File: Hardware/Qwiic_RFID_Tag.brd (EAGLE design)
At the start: 30.5 x 44.5 mm, 50 parts, among them J1 Qwiic, J2 Qwiic, U1 ST25DV64KC

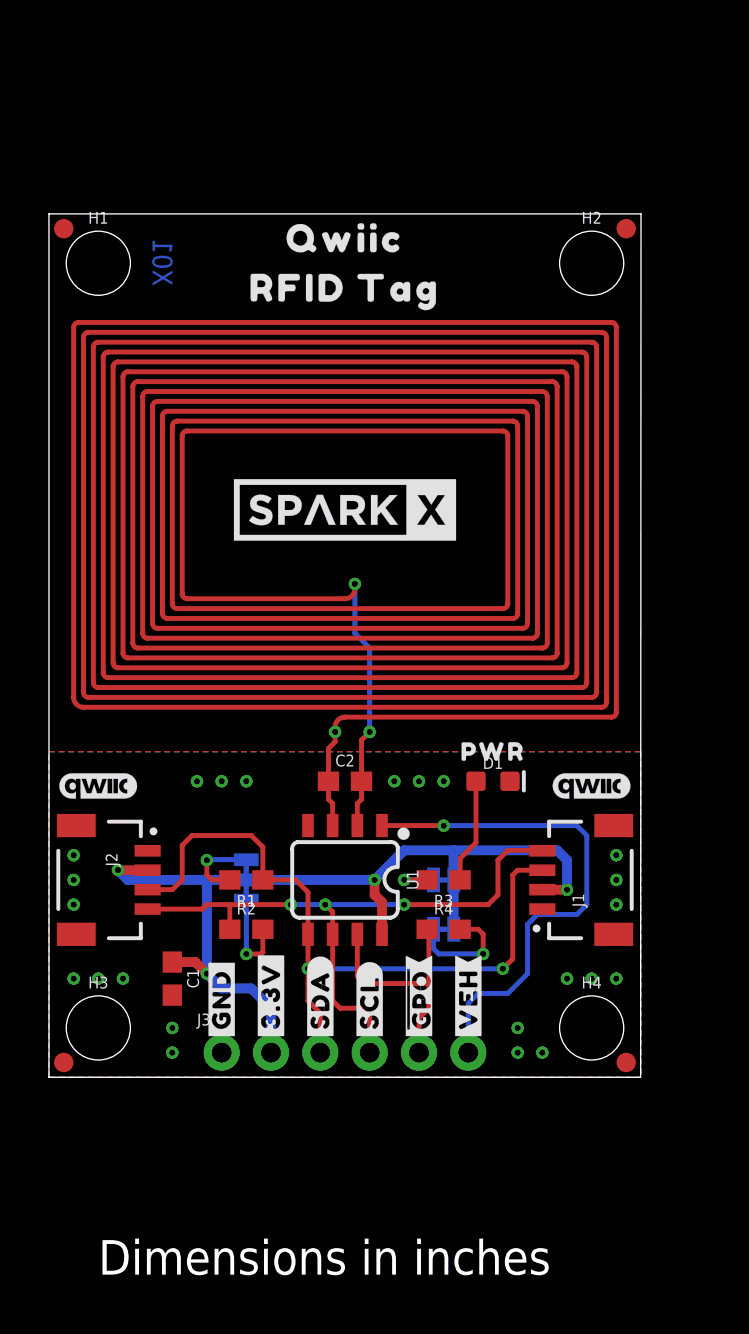
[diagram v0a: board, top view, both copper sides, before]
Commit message: Fixed fiducial placement, board version size and polygon isolation.
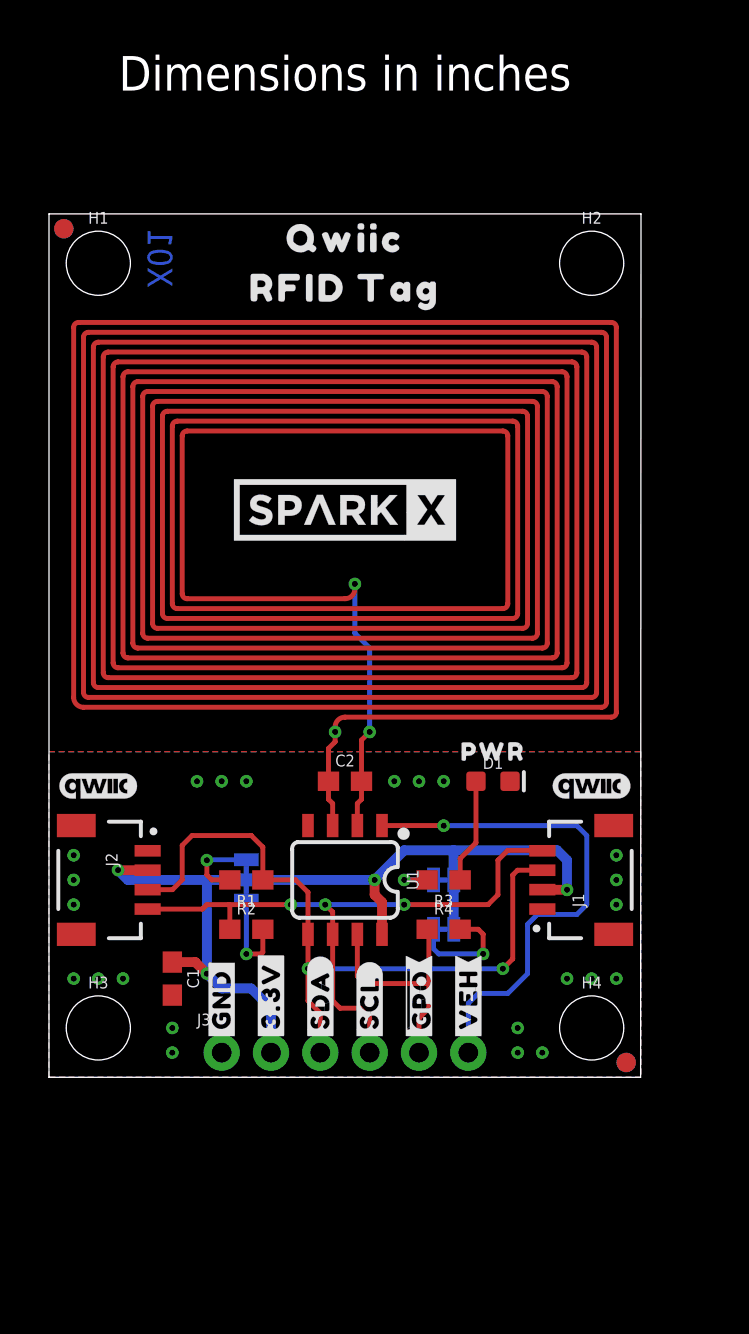
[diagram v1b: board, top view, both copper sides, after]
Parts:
- moved FD1 29.0 mm to (0.76, 43.7), flipped to the bottom
- moved FD3 29.0 mm to (29.7, 0.76), flipped to the bottom
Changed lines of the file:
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@@
 <drawing>
 <settings>
-<setting alwaysvectorfont="no"/>
+<setting alwaysvectorfont="yes"/>
 <setting verticaltext="up"/>
 </settings>
-<grid distance="0.05" unitdist="inch" unit="inch" style="lines" multiple="1" display="yes" altdistance="0.005" altunitdist="inch" altunit="inch"/>
+<grid distance="0.1" unitdist="inch" unit="inch" style="lines" multiple="1" display="yes" altdistance="0.005" altunitdist="inch" altunit="inch"/>
 <layers>
 <layer number="1" name="Top" color="4" fill="1" visible="yes" active="yes"/>
@@
 <wire x1="30.48" y1="44.45" x2="0" y2="44.45" width="0" layer="20"/>
 <wire x1="0" y1="44.45" x2="0" y2="0" width="0" layer="20"/>
-<dimension x1="0" y1="-2.54" x2="30.48" y2="-2.54" x3="15.24" y3="-5.08" textsize="1.778" textratio="15" layer="20" dtype="horizontal" unit="inch"/>
-<dimension x1="-2.54" y1="44.45" x2="-2.54" y2="0" x3="-5.08" y3="22.225" textsize="1.778" textratio="15" layer="20" dtype="vertical" unit="inch"/>
-<text x="2.54" y="-10.16" size="1.778" layer="20" font="vector" ratio="15">Dimensions in inches</text>
-<dimension x1="2.54" y1="46.99" x2="27.94" y2="46.99" x3="15.24" y3="48.26" textsize="1.778" textratio="15" layer="20" dtype="horizontal" unit="inch"/>
-<text x="6.35" y="43.18" size="1.016" layer="16" font="vector" ratio="15" rot="MR270">X01</text>
-<dimension x1="34.29" y1="2.54" x2="34.29" y2="41.91" x3="36.83" y3="22.225" textsize="1.778" textratio="15" layer="20" unit="inch"/>
+<dimension x1="0" y1="-1.27" x2="30.48" y2="-1.27" x3="15.24" y3="-3.81" textsize="1.778" textratio="15" layer="20" dtype="horizontal" unit="inch"/>
+<dimension x1="-1.27" y1="44.45" x2="-1.27" y2="0" x3="-3.81" y3="22.225" textsize="1.778" textratio="15" layer="20" dtype="vertical" unit="inch"/>
+<text x="15.24" y="50.8" size="1.778" layer="20" font="vector" ratio="15" align="bottom-center">Dimensions in inches</text>
+<dimension x1="2.54" y1="45.72" x2="27.94" y2="45.72" x3="15.24" y3="46.99" textsize="1.778" textratio="15" layer="20" dtype="horizontal" unit="inch"/>
+<dimension x1="31.75" y1="2.54" x2="31.75" y2="41.91" x3="34.29" y3="22.225" textsize="1.778" textratio="15" layer="20" unit="inch"/>
+<text x="5.08" y="40.64" size="1.27" layer="16" font="vector" ratio="15" rot="MR90">X01</text>
 </plain>
 <attributes>
@@
 <attribute name="VALUE" x="20.32" y="6.858" size="0.6096" layer="27" font="vector" ratio="20" align="top-center"/>
 </element>
-<element name="FD1" library="SparkFun-Aesthetics" package="FIDUCIAL-1X2" value="FIDUCIAL1X2" x="29.718" y="43.688" smashed="yes"/>
+<element name="FD1" library="SparkFun-Aesthetics" package="FIDUCIAL-1X2" value="FIDUCIAL1X2" x="0.762" y="43.688" smashed="yes" rot="MR0"/>
 <element name="FD2" library="SparkFun-Aesthetics" package="FIDUCIAL-1X2" value="FIDUCIAL1X2" x="0.762" y="43.688" smashed="yes"/>
-<element name="FD3" library="SparkFun-Aesthetics" package="FIDUCIAL-1X2" value="FIDUCIAL1X2" x="0.762" y="0.762" smashed="yes"/>
+<element name="FD3" library="SparkFun-Aesthetics" package="FIDUCIAL-1X2" value="FIDUCIAL1X2" x="29.718" y="0.762" smashed="yes" rot="MR0"/>
 <element name="FD4" library="SparkFun-Aesthetics" package="FIDUCIAL-1X2" value="FIDUCIAL1X2" x="29.718" y="0.762" smashed="yes"/>
 <element name="LOGO1" library="SparkFun-Aesthetics" package="OSHW-LOGO-MINI" value="OSHW-LOGOMINI" x="24.384" y="41.91" smashed="yes" rot="MR0"/>
@@
 <contactref element="U1" pad="4"/>
 <contactref element="J3" pad="1"/>
-<polygon width="0.2032" layer="1" isolate="0.3048">
+<polygon width="0.2032" layer="1" isolate="0.254">
 <vertex x="0" y="0"/>
 <vertex x="0" y="16.764"/>
@@
 <vertex x="30.48" y="0"/>
 </polygon>
-<polygon width="0.2032" layer="16" isolate="0.3048">
+<polygon width="0.2032" layer="16" isolate="0.254">
 <vertex x="0" y="16.764"/>
 <vertex x="30.48" y="16.764"/>
